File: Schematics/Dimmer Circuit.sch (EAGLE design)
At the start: 7 parts

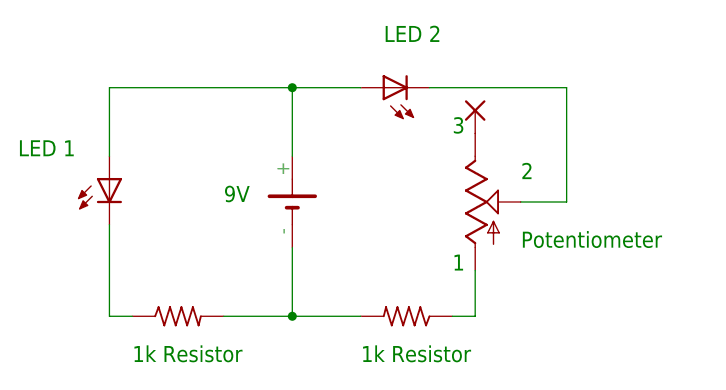
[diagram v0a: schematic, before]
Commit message: Cleaned up schematics' labeling.
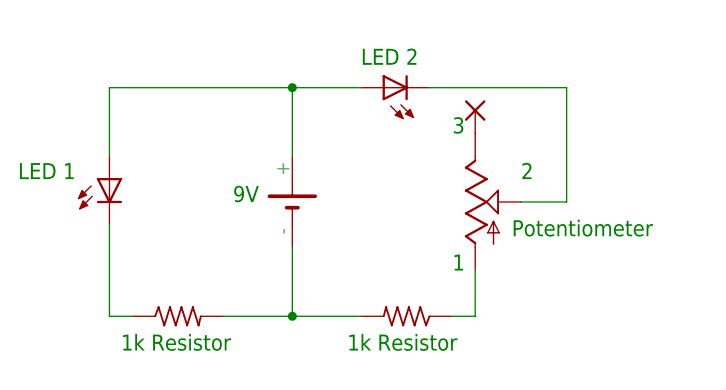
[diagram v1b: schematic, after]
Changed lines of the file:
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@@
 <?xml version="1.0" encoding="utf-8"?>
 <!DOCTYPE eagle SYSTEM "eagle.dtd">
-<eagle version="6.6.0">
+<eagle version="9.4.2">
 <drawing>
 <settings>
 <setting alwaysvectorfont="no"/>
+<setting keepoldvectorfont="yes"/>
 <setting verticaltext="up"/>
 </settings>
@@
 <sheet>
 <plain>
-<text x="5.08" y="68.58" size="1.778" layer="91">9V</text>
-<text x="-5.08" y="50.8" size="1.778" layer="91">1k Resistor</text>
-<text x="20.32" y="50.8" size="1.778" layer="91">1k Resistor</text>
-<text x="-17.78" y="73.66" size="1.778" layer="91">LED 1</text>
-<text x="22.86" y="86.36" size="1.778" layer="91">LED 2</text>
-<text x="38.1" y="63.5" size="1.778" layer="91">Potentiometer</text>
+<text x="6.096" y="68.58" size="1.778" layer="91">9V</text>
+<text x="-6.35" y="52.07" size="1.778" layer="91">1k Resistor</text>
+<text x="18.796" y="52.07" size="1.778" layer="91">1k Resistor</text>
+<text x="-17.78" y="71.12" size="1.778" layer="91">LED 1</text>
+<text x="20.32" y="83.82" size="1.778" layer="91">LED 2</text>
+<text x="37.084" y="64.77" size="1.778" layer="91">Potentiometer</text>
 <text x="30.48" y="60.96" size="1.778" layer="91">1</text>
 <text x="38.1" y="71.12" size="1.778" layer="91">2</text>
@@
 </sheet>
 </sheets>
+<errors>
+</errors>
 </schematic>
 </drawing>
